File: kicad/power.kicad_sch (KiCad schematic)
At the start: 38 parts, among them Q201 AOD409, U201 TPS54331, U202 AMS1117-3.3

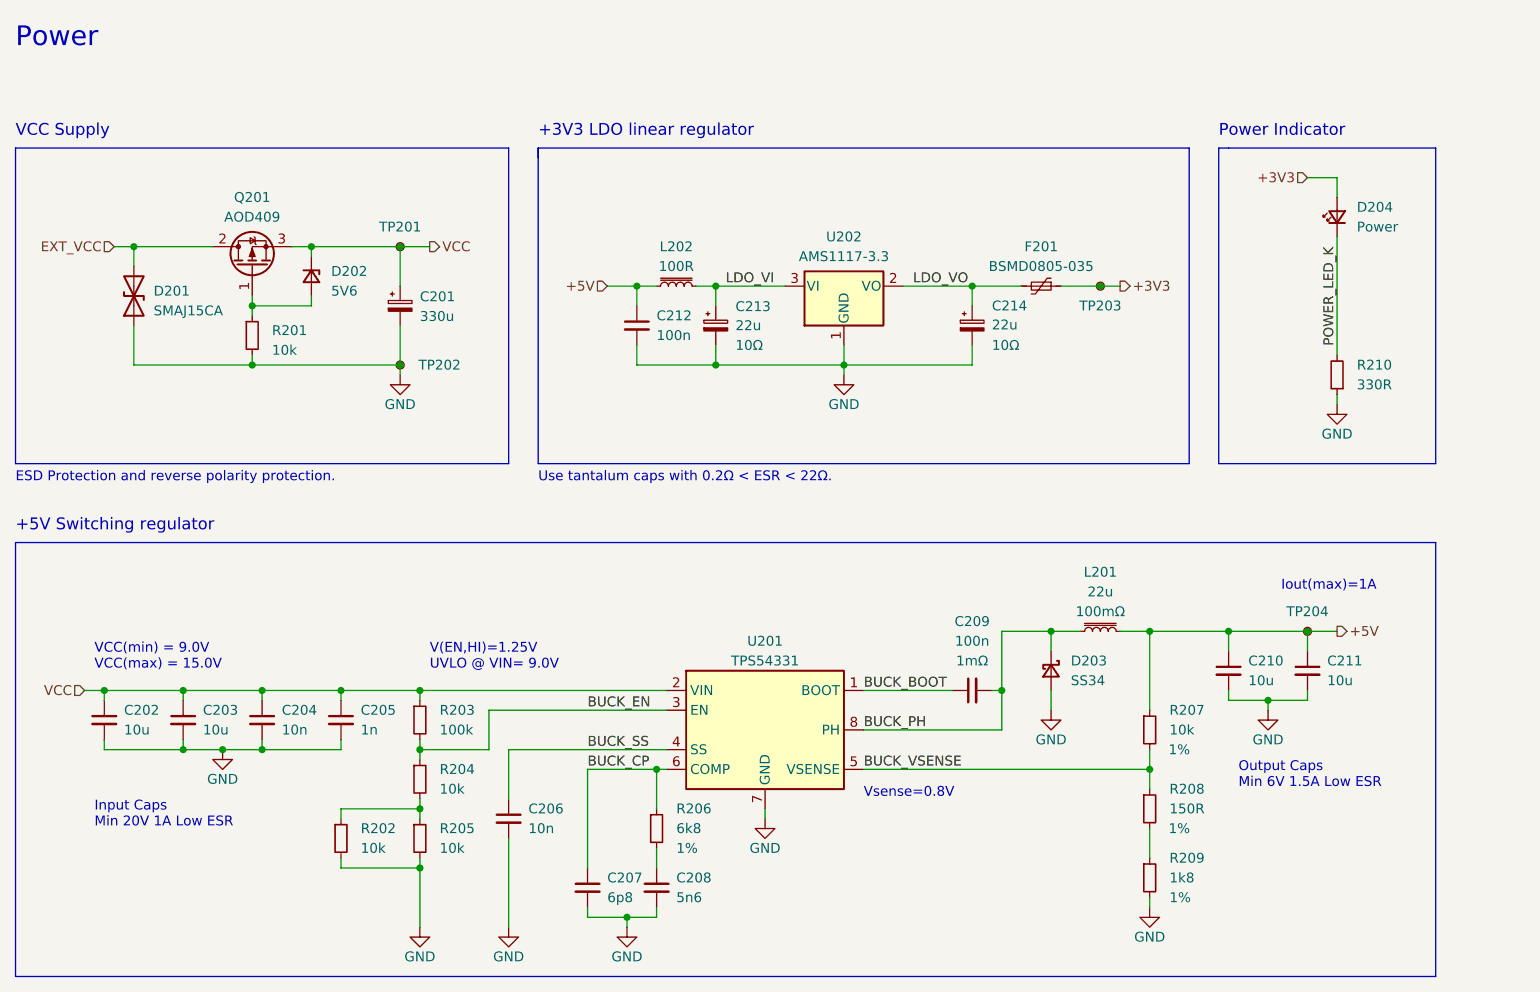
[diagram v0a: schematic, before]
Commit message: Add PTC fuses on lights drivers and before switching regulator.
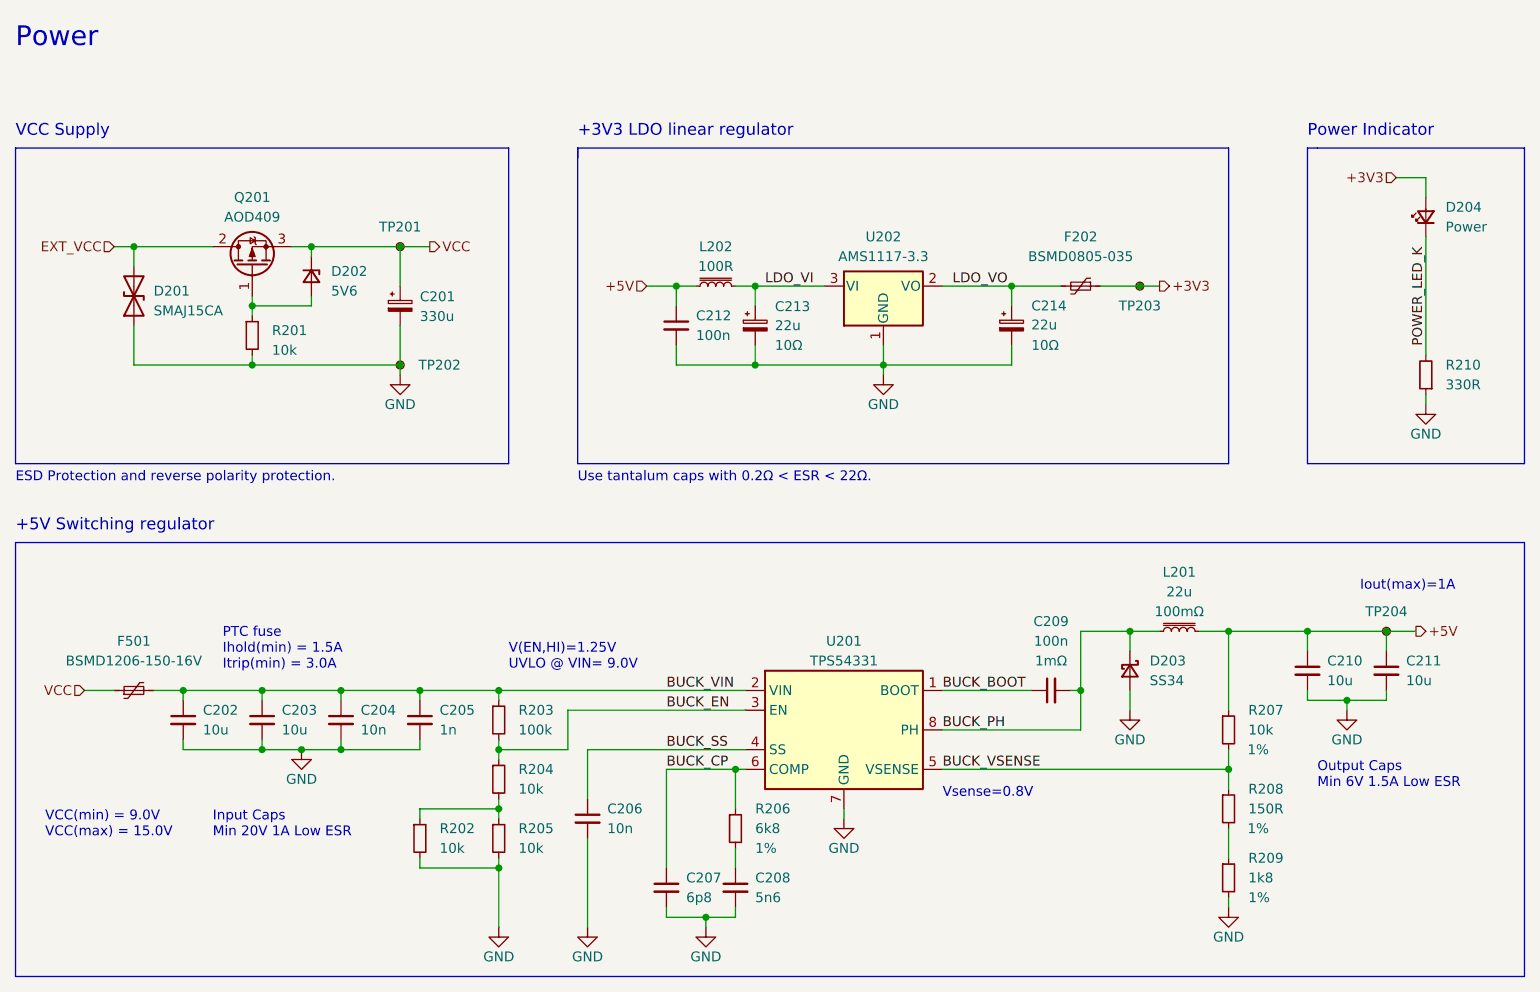
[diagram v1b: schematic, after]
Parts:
- added F501: BSMD1206-150-16V, Fuse:Fuse_1206_3216Metric_Pad1.42x1.75mm_HandSolder, symbol Device:Polyfuse_Small
- renumbered F201 to F202
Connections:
- net VCC: now also F501.1; no longer C202.1, C203.1, C204.1, C205.1, R203.1, U201.2 (VIN)
- new net BUCK_VIN: C202.1, C203.1, C204.1, C205.1, F501.2, R203.1, U201.2 (VIN)
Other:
- note added: "PTC fuse Ihold(min) = 1.5A Itrip(min) = 3.0A"
- moved on the sheet: C202, C203, C204, C205, C206, C207, C208, C209, C210, C211, C212, C213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
